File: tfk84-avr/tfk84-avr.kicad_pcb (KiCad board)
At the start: 4 copper layers, 304.8 x 114.3 mm, 334 parts, among them J1 USB_C_Receptacle_USB2.0, J2 AVR-ISP-6, SW1 Reset, U1 ATmega32U4-AU, U2 IS31FL3733B-TQLS4-TR, U3 IS31FL3733B-TQLS4-TR, Y1 16MHz

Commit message: Continue layout
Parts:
- added H10: MountingHole, MountingHole:MountingHole_2.5mm_Pad, F.Cu at (243.1, 133.0)
- added H11: MountingHole, MountingHole:MountingHole_2.5mm_Pad, F.Cu at (249.6, 133.0)
- added H9: MountingHole, MountingHole:MountingHole_2.5mm_Pad, F.Cu at (236.5, 133.0)
- D16, D17, D18, D19, D20, D21, D22, D23, D24, D25, D26, D27, D28, D29, D30, D31, D32, D33, D34, D35, D36, D37, D38, D39, D40, D41, D42, D43, D44, D45, D46, D47, D48, D49, D50, D51, D52, D53, D54, D55, D56, D57, D58, D59, D60, D61, D62, D63, D64, D65, D66, D67, D68, D69, D70, D71, D72, D73, D74, D75, D76, D77, D78, D79, D80, D81, D82, D83, D84, D85, D86, D87, D88, D89, D90, D91, D92, D93, D94, D95, D96, D97, D98, D99, J1: moved to B.Cu
- moved D67 662.0 mm to (686.6, 138.9), turned to 180 degrees
- moved D68 638.2 mm to (686.6, 158.0), turned to 180 degrees
- moved D78 628.5 mm to (658.0, 138.9), turned to 180 degrees
- moved D69 616.7 mm to (686.6, 177.0), turned to 180 degrees
- moved D70 597.7 mm to (686.6, 196.1), turned to 180 degrees
- moved D62 586.2 mm to (610.4, 119.9), turned to 180 degrees
- moved D63 582.7 mm to (629.4, 119.9), turned to 180 degrees
- moved D71 581.4 mm to (686.6, 215.1), turned to 180 degrees
- moved D64 579.9 mm to (648.5, 119.9), turned to 180 degrees
- moved D65 577.8 mm to (667.5, 119.9), turned to 180 degrees
- moved D88 576.5 mm to (605.6, 177.0), turned to 180 degrees
- moved D77 565.3 mm to (629.4, 138.9), turned to 180 degrees
- moved D66 561.7 mm to (686.6, 119.9), turned to 180 degrees
- moved D85 552.9 mm to (662.8, 158.0), turned to 180 degrees
- moved D98 551.3 mm to (641.4, 196.1), turned to 180 degrees
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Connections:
- D65 pad 3: Net-(D65-Pad3) -> /tfk84 RGB Matrix/tfk84 AVR RGB Matrix Slave/S_SW3
- D66 pad 3: Net-(D65-Pad3) -> /tfk84 RGB Matrix/tfk84 AVR RGB Matrix Slave/S_SW3
- D67 pad 3: Net-(D65-Pad3) -> /tfk84 RGB Matrix/tfk84 AVR RGB Matrix Slave/S_SW3
- D68 pad 3: Net-(D65-Pad3) -> /tfk84 RGB Matrix/tfk84 AVR RGB Matrix Slave/S_SW3
- D69 pad 3: Net-(D65-Pad3) -> /tfk84 RGB Matrix/tfk84 AVR RGB Matrix Slave/S_SW3
- D70 pad 3: Net-(D65-Pad3) -> /tfk84 RGB Matrix/tfk84 AVR RGB Matrix Slave/S_SW3
- D71 pad 3: Net-(D65-Pad3) -> /tfk84 RGB Matrix/tfk84 AVR RGB Matrix Slave/S_SW3
- D72 pad 4: Net-(D72-Pad4) -> /tfk84 RGB Matrix/tfk84 AVR RGB Matrix Slave/S_CS1
- D73 pad 4: Net-(D73-Pad4) -> /tfk84 RGB Matrix/tfk84 AVR RGB Matrix Slave/S_CS3
- D86 pad 4: Net-(D72-Pad4) -> /tfk84 RGB Matrix/tfk84 AVR RGB Matrix Slave/S_CS1
- D87 pad 4: Net-(D73-Pad4) -> /tfk84 RGB Matrix/tfk84 AVR RGB Matrix Slave/S_CS3

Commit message: Continue layout
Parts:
- D10, D11, D12, D13, D14, D15, D4, D5, D6, D7, D8, D9, J2, SW1, Y1: moved to B.Cu
- H1: renamed from H2; footprint MountingHole:MountingHole_2.5mm_Pad -> MountingHole:MountingHole_2.5mm_Pad_TopOnly
- H10, H11, H3, H4, H9: footprint MountingHole:MountingHole_2.5mm_Pad -> MountingHole:MountingHole_2.5mm_Pad_TopOnly
- H2: renamed from H1; footprint MountingHole:MountingHole_2.5mm_Pad -> MountingHole:MountingHole_2.5mm_Pad_TopOnly
- moved D9 317.9 mm to (537.4, 300.0), turned to 180 degrees
- moved D8 312.4 mm to (522.3, 300.0), turned to 180 degrees
- moved D5 303.9 mm to (476.6, 300.0), turned to 180 degrees
- moved D7 299.5 mm to (506.0, 300.0), turned to 180 degrees
- moved D10 297.3 mm to (537.8, 282.2)
- moved D6 296.7 mm to (490.5, 300.0), turned to 180 degrees
- moved Y1 294.1 mm to (505.2, 215.1), turned to 90 degrees
- moved D11 293.5 mm to (522.3, 282.2)
- moved D12 293.0 mm to (506.0, 282.2)
- moved D4 292.0 mm to (461.2, 300.0), turned to 180 degrees
- moved D13 283.9 mm to (490.5, 282.2)
- moved D15 278.6 mm to (461.2, 282.2)
- moved D14 275.6 mm to (476.6, 282.2)
- moved H4 232.1 mm to (453.2, 196.1)
- moved H2 200.6 mm to (429.4, 129.4)
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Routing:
- added copper zone on PWR, net +5V
- added copper zone on GND, net GND

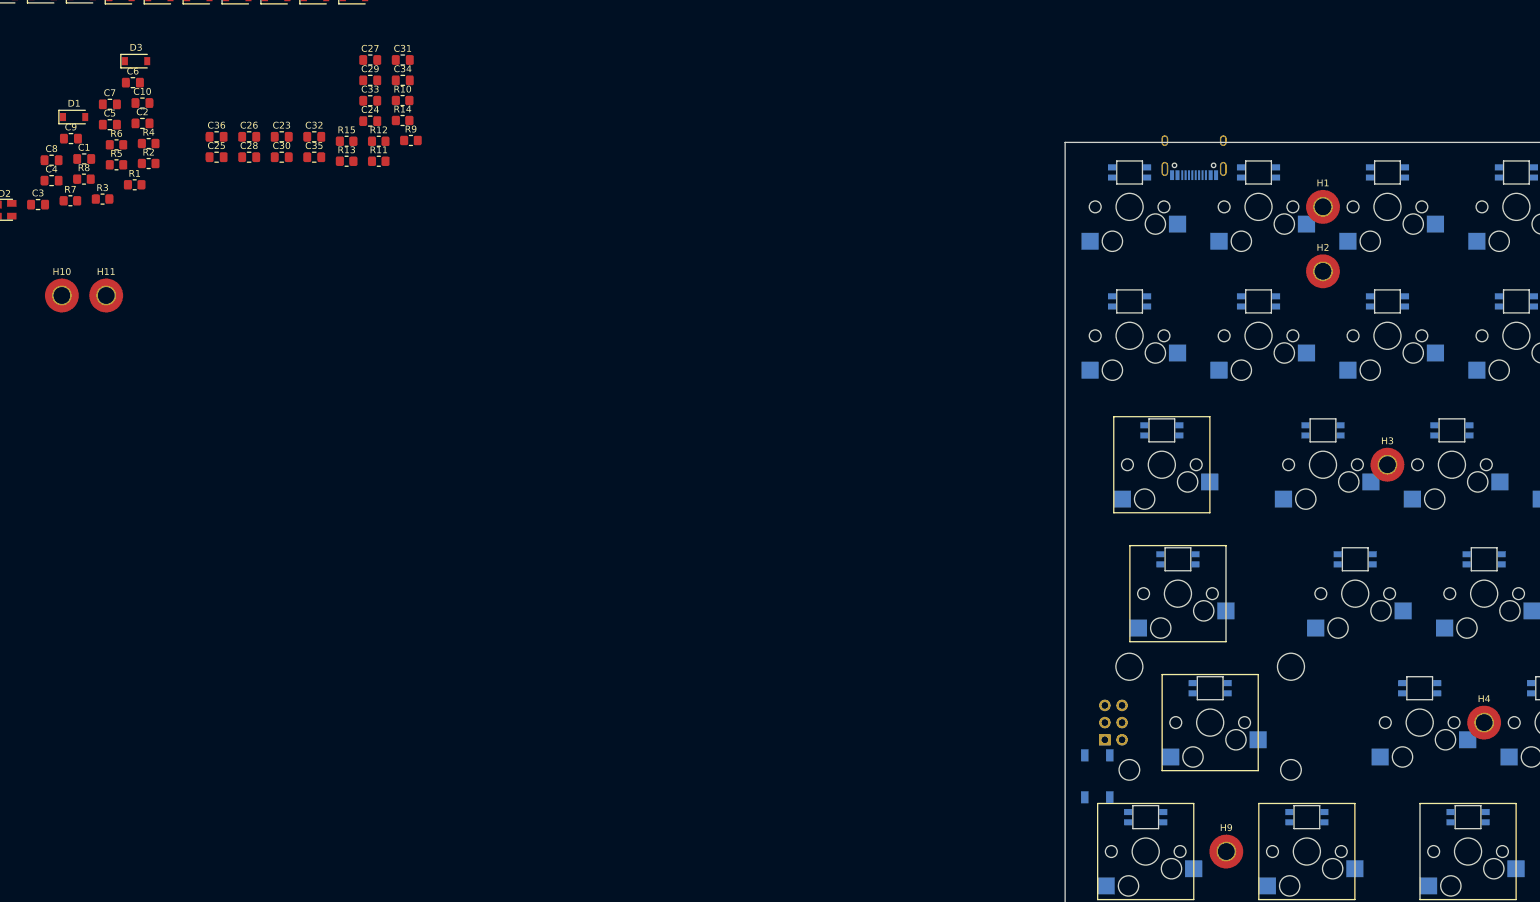
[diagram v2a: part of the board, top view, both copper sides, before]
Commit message: Begin placing mounting holes
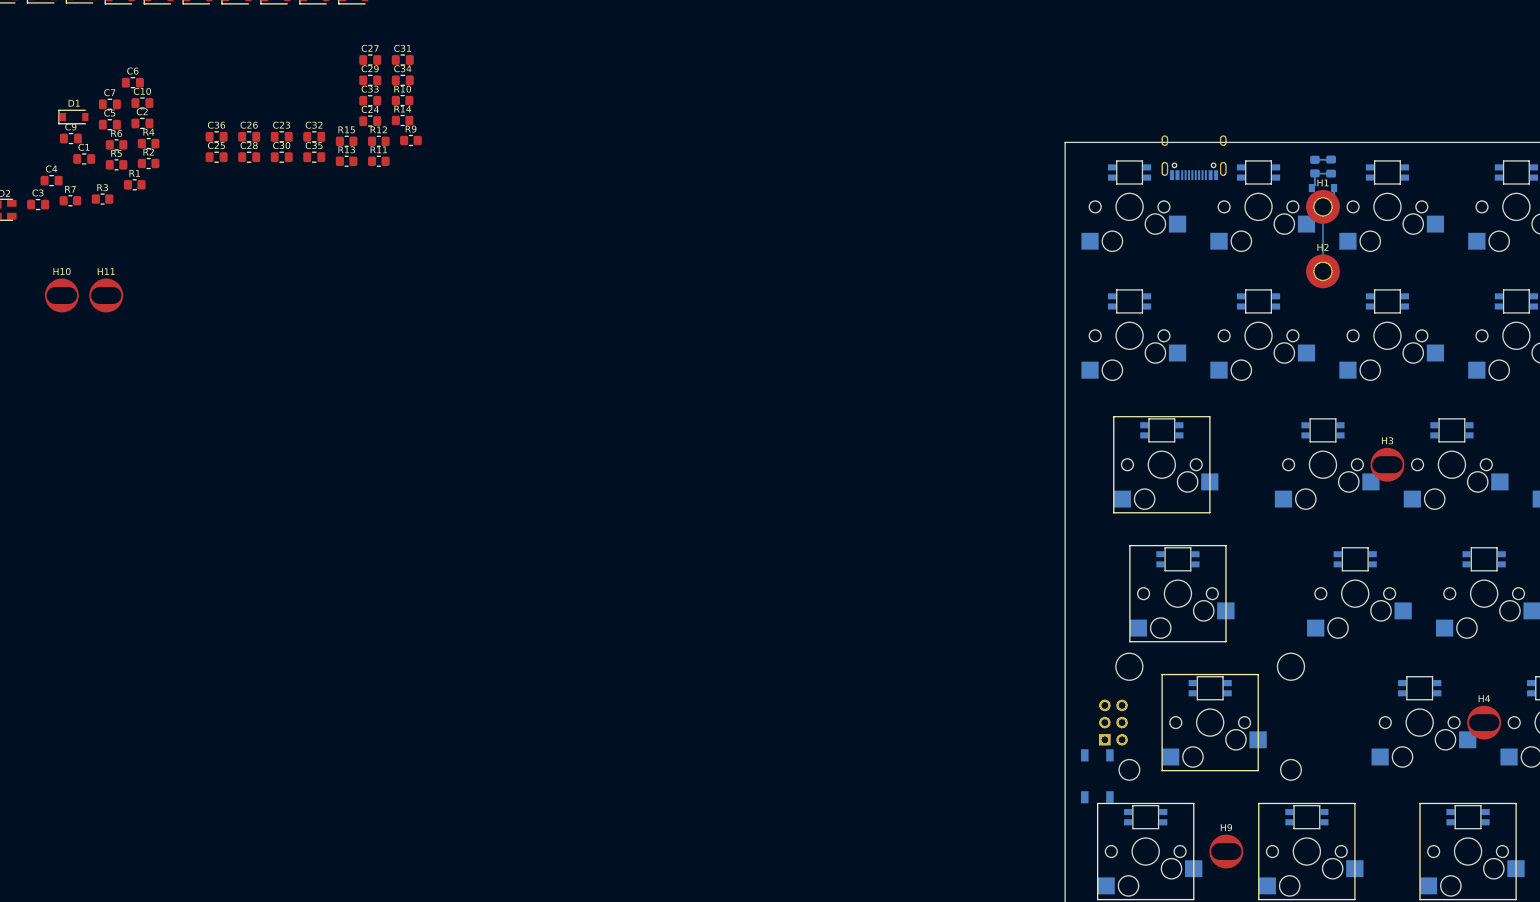
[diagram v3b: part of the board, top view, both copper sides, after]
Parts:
- C8, D3, R8: moved to B.Cu
- H1: footprint MountingHole:MountingHole_2.5mm_Pad_TopOnly -> random-keyboard-parts:MountingHole_2.5mm_Pad_TopOnly_NoCrtYd
- H10, H11, H3, H4, H9: footprint MountingHole:MountingHole_2.5mm_Pad_TopOnly -> random-keyboard-parts:MountingHole_4.5x2.5mm_Pad_TopOnly_NPTH
- H2: value MountingHole -> Case; footprint MountingHole:MountingHole_2.5mm_Pad_TopOnly -> random-keyboard-parts:MountingHole_2.5mm_Pad_TopOnly_NoCrtYd
- MX38, MX62: footprint Switch_Keyboard_Kailh:SW_Hotswap_Kailh_1.00u_NoFrontSilk -> random-keyboard-parts:SW_Hotswap_Kailh_1.00u_NoFrontSilk_CornerPad
- moved C8 189.0 mm to (430.6, 113.9), turned to 90 degrees
- moved R8 181.9 mm to (428.2, 113.9), turned to 90 degrees
- moved D3 176.4 mm to (429.4, 117.1)
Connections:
- H2 pad 1: (no net) -> Net-(D3-Pad2)
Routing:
- net Net-(D3-Pad2): track 0.00 -> 13.0 mm
- net Net-(C8-Pad1): track 0.00 -> 4.76 mm
- net /SHIELD: track 0.00 -> 2.40 mm

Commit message: Continue layout
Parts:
- moved D36 332.6 mm to (193.3, 130.2)
- moved D60 332.6 mm to (240.9, 92.1)
- moved D65 332.6 mm to (336.2, 92.1)
- moved D74 332.6 mm to (240.9, 111.1)
- moved D83 332.6 mm to (288.5, 130.2)
- moved D90 332.6 mm to (324.2, 149.2)
- moved D91 332.6 mm to (336.2, 168.3)
- moved D92 332.6 mm to (336.2, 187.3)
- moved D93 332.6 mm to (217.1, 149.2)
- moved D96 332.6 mm to (264.7, 168.3)
- moved H6 332.6 mm to (324.2, 149.2)
- moved MX11 332.6 mm to (336.2, 92.1)
- moved MX19 332.6 mm to (240.9, 92.1)
- moved MX31 332.6 mm to (240.9, 111.1)
- moved MX33 332.6 mm to (288.5, 130.2)
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
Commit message: Add mounting holes for XD84 and KBD75V2 cases
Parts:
- removed the H5 at (326.6, 111.1)
- added H10: MountingHole, random-keyboard-parts:MountingHole_4.5x2.5mm_Pad_TopOnly_NPTH, F.Cu at (345.7, 139.7)
- added H11: MountingHole, random-keyboard-parts:MountingHole_4.5x2.5mm_Pad_TopOnly_NPTH, F.Cu at (188.5, 149.2)
- added H12: MountingHole, random-keyboard-parts:MountingHole_4.5x2.5mm_Pad_TopOnly_NPTH, F.Cu at (121.8, 168.3)
- added H13: MountingHole, random-keyboard-parts:MountingHole_4.5x2.5mm_Pad_TopOnly_NPTH, F.Cu at (345.7, 177.8)
- added H14: MountingHole, random-keyboard-parts:MountingHole_4.5x2.5mm_Pad_TopOnly_NPTH, F.Cu at (83.7, 187.3)
- added H15: MountingHole, random-keyboard-parts:MountingHole_4.5x2.5mm_Pad_TopOnly_NPTH, F.Cu at (248.4, 187.3)
- added H16: MountingHole, random-keyboard-parts:MountingHole_4.5x2.5mm_Pad_TopOnly_NPTH, F.Cu at (326.6, 187.3)
- added H18: Backspace stabilizer, Mounting_Keyboard_Stabilizer:Stabilizer_Cherry_MX_2u_CrtYd, F.Cu at (326.6, 111.1)
- added H7: MountingHole, random-keyboard-parts:MountingHole_4.5x2.5mm_Pad_TopOnly_NPTH, F.Cu at (83.7, 130.2)
- added H8: MountingHole, random-keyboard-parts:MountingHole_4.5x2.5mm_Pad_TopOnly_NPTH, F.Cu at (107.6, 130.2)
- MX38, MX62: footprint random-keyboard-parts:SW_Hotswap_Kailh_1.00u_NoFrontSilk_CornerPad -> Switch_Keyboard_Kailh:SW_Hotswap_Kailh_1.00u_NoFrontSilk
- moved H5 260.9 mm to (326.6, 92.1)
- moved H9 216.6 mm to (221.9, 130.2)
- moved H4 149.5 mm to (250.4, 92.1)
- moved H6 102.7 mm to (326.6, 101.6)
- moved H3 76.8 mm to (174.2, 92.1)
- renumbered H6 to H19, H7 to H20, H8 to H21, H9 to H5, H10 to H6, H11 to H9

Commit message: Tweak holes
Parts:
- D1, F1: moved to B.Cu
- H1, H2: footprint random-keyboard-parts:MountingHole_2.5mm_Pad_TopOnly_NoCrtYd -> MountingHole:MountingHole_2.5mm_Pad
- MX14: footprint Switch_Keyboard_Kailh:SW_Hotswap_Kailh_1.00u_NoFrontSilk -> random-keyboard-parts:SW_Hotswap_Kailh_1.00u_NoFrontSilk_CornerPad_TightCrtYd
- moved D1 340.1 mm to (92.5, 102.8), turned to 180 degrees
- moved F1 323.2 mm to (92.5, 100.4), turned to 180 degrees
- moved C8 3.66 mm to (95.6, 86.9)
- moved D3 3.37 mm to (100.4, 86.9), turned to 270 degrees
- moved R8 1.43 mm to (98.0, 86.9)
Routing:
- net Net-(D3-Pad2): track 13.0 -> 4.50 mm
- net Net-(C8-Pad1): track 4.76 -> 6.03 mm

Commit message: Place switch diodes
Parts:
- C1, C10, C2, C3, C4, C5, C6, C7, C9, D100, D101, D102, D103, D104, D105, D106, D107, D108, D109, D110, D111, D112, D113, D114, D115, D116, D117, D118, D119, D120, D121, D122, D123, D124, D125, D126, D127, D128, D129, D130, D131, D132, D133, D134, D135, D136, D137, D138, D139, D140, D141, D142, D143, D144, D145, D146, D147, D148, D149, D150, D151, D152, D153, D154, D155, D156, D157, D158, D159, D160, D161, D162, D163, D164, D165, D166, D167, D168, D169, D170, D171, D172, D173, D174, D175, D176, D177, D178, D179, D180, D181, D182, D183, D2, R2, R3, R4, R5, R6, R7: moved to B.Cu
- moved D148 489.3 mm to (63.1, 191.7), turned to 90 degrees
- moved D124 475.7 mm to (73.8, 157.6), turned to 180 degrees
- moved D112 475.7 mm to (69.5, 138.5), turned to 180 degrees
- moved D136 474.8 mm to (76.6, 176.6), turned to 180 degrees
- moved D137 460.8 mm to (93.3, 138.5), turned to 180 degrees
- moved D149 451.6 mm to (98.0, 157.6), turned to 180 degrees
- moved D150 440.4 mm to (117.1, 157.6), turned to 180 degrees
- moved D101 423.2 mm to (64.7, 100.4), turned to 180 degrees
- moved D138 422.2 mm to (112.3, 138.5), turned to 180 degrees
- moved D15 421.5 mm to (79.0, 104.4)
- moved D139 411.0 mm to (131.4, 138.5), turned to 180 degrees
- moved D103 404.3 mm to (140.9, 100.4), turned to 180 degrees
- moved D115 398.7 mm to (140.9, 119.5), turned to 180 degrees
- moved D100 398.0 mm to (64.7, 119.5), turned to 180 degrees
- moved D4 396.6 mm to (83.7, 178.2)
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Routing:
- net VBUS: track 0.00 -> 26.9 mm
- net +5V: track 0.00 -> 6.45 mm, vias 0 -> 2
- net /SHIELD: track 2.40 -> 6.51 mm
- net GND: track 0.00 -> 3.71 mm, vias 0 -> 1
- net Net-(D3-Pad2): track 4.50 -> 5.88 mm

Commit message: Continue layout
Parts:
- C11, C12, C23, C24, C25, C26, C27, C28, C29, C30, C31, C32, C33, C34, C35, C36, R1, R10, R11, R12, R13, R14, R15, R9: moved to B.Cu
- moved C12 559.3 mm to (34.5, 148.8), turned to 270 degrees
- moved C11 523.1 mm to (88.5, 181.4), turned to 270 degrees
- moved R1 388.8 mm to (64.7, 181.8)
- moved R10 312.7 mm to (205.6, 218.3), turned to 270 degrees
- moved R11 307.2 mm to (205.6, 222.2), turned to 90 degrees
- moved R9 304.4 mm to (213.9, 219.9), turned to 90 degrees
- moved C27 301.0 mm to (218.3, 219.1)
- moved C24 298.1 mm to (208.0, 203.6), turned to 180 degrees
- moved C34 297.3 mm to (227.8, 222.6)
- moved R12 292.7 mm to (223.4, 221.5), turned to 90 degrees
- moved C33 290.5 mm to (227.8, 220.7)
- moved R14 287.0 mm to (243.8, 234.2)
- moved C35 285.5 mm to (218.3, 217.1)
- moved C31 285.2 mm to (238.9, 214.7)
- moved C23 284.5 mm to (208.0, 201.6), turned to 180 degrees
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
